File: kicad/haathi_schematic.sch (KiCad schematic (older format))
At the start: 0 parts

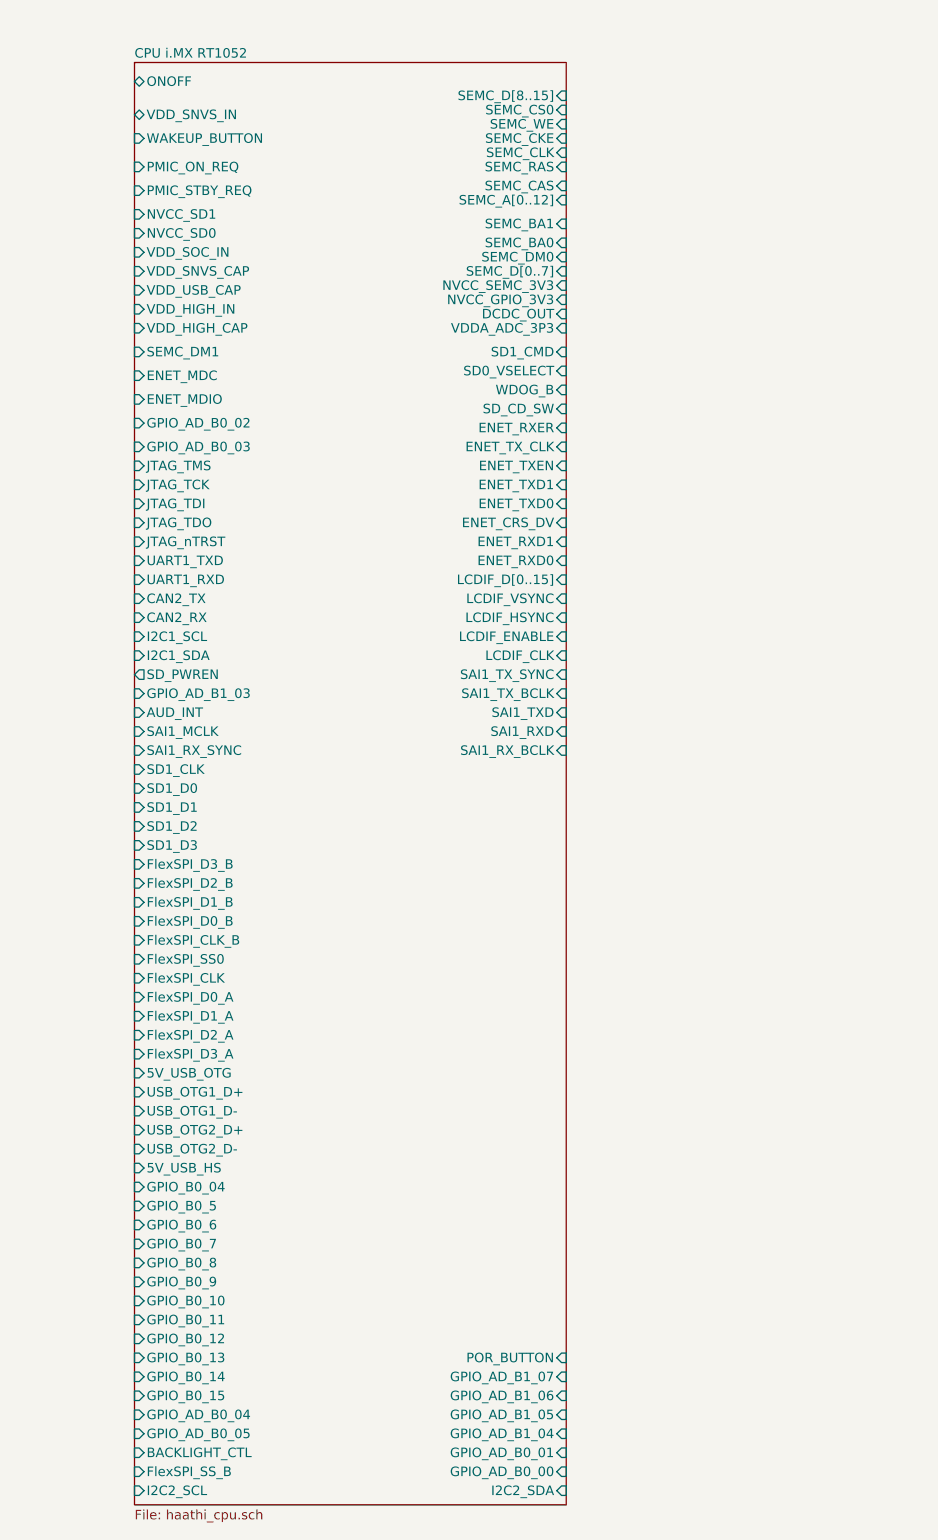
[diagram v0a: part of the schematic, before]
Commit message: Top schematic, re-arranged CPU block pins and added wires
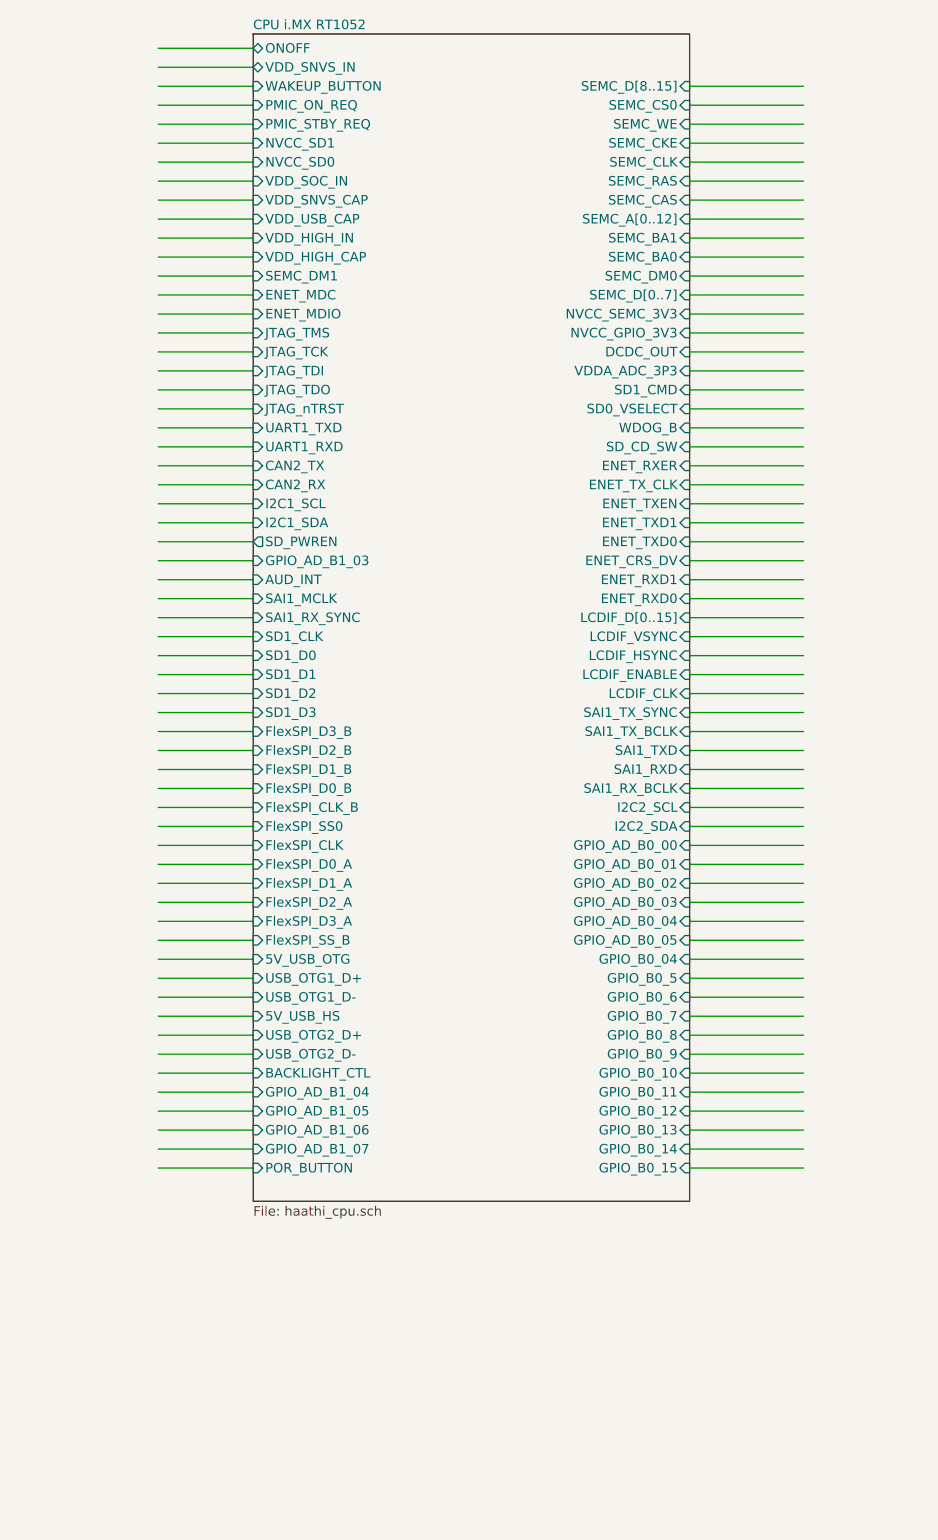
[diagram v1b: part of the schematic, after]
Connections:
- wire segments 5 -> 123

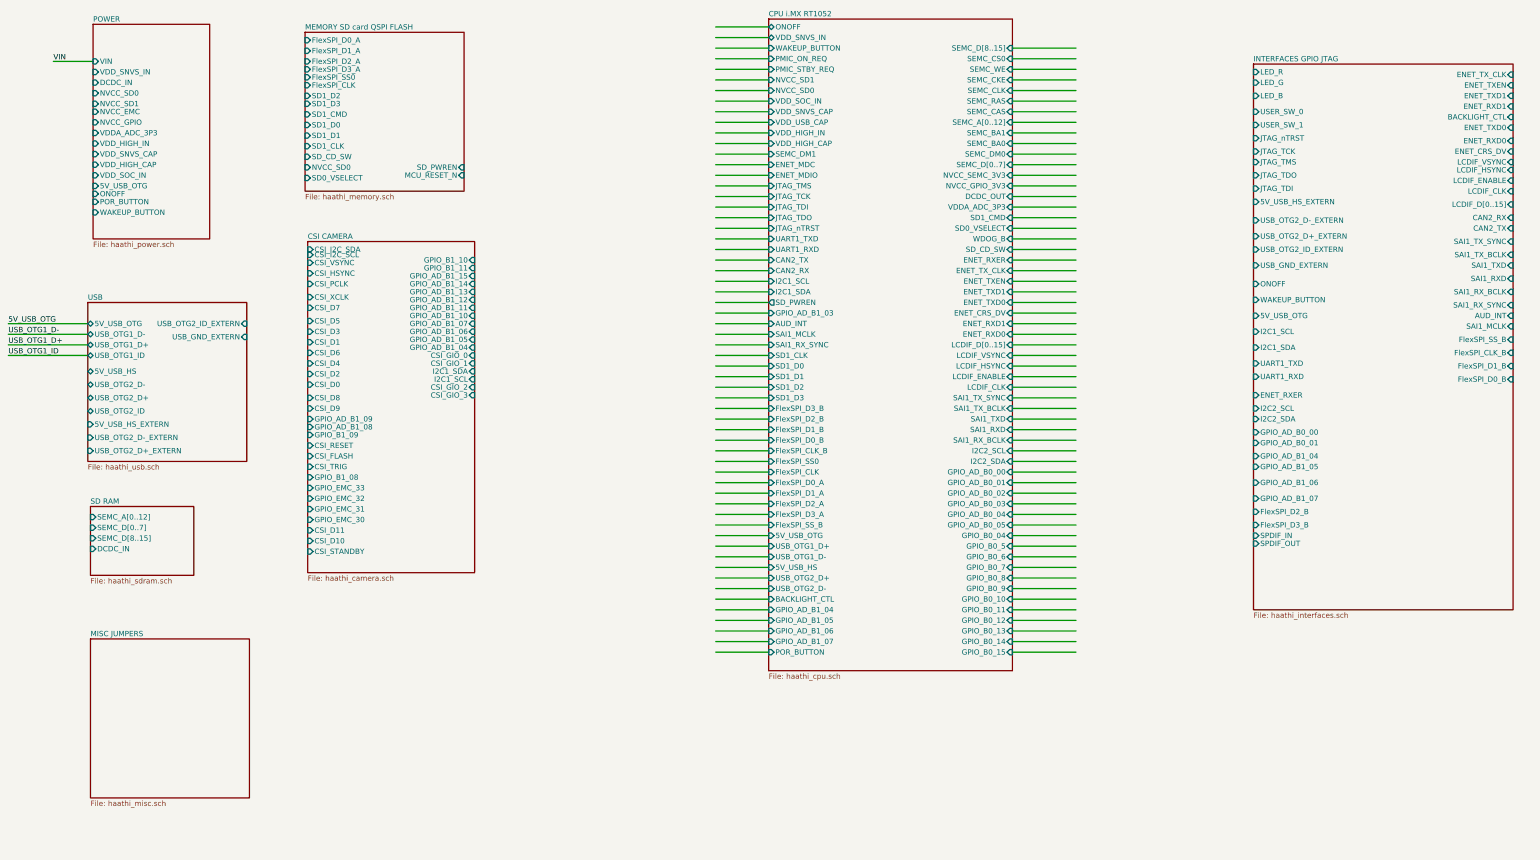
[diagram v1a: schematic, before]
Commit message: CPU, Interfaces, SDRAM top sheet wiring done, CPU bootcfg local labels fixed
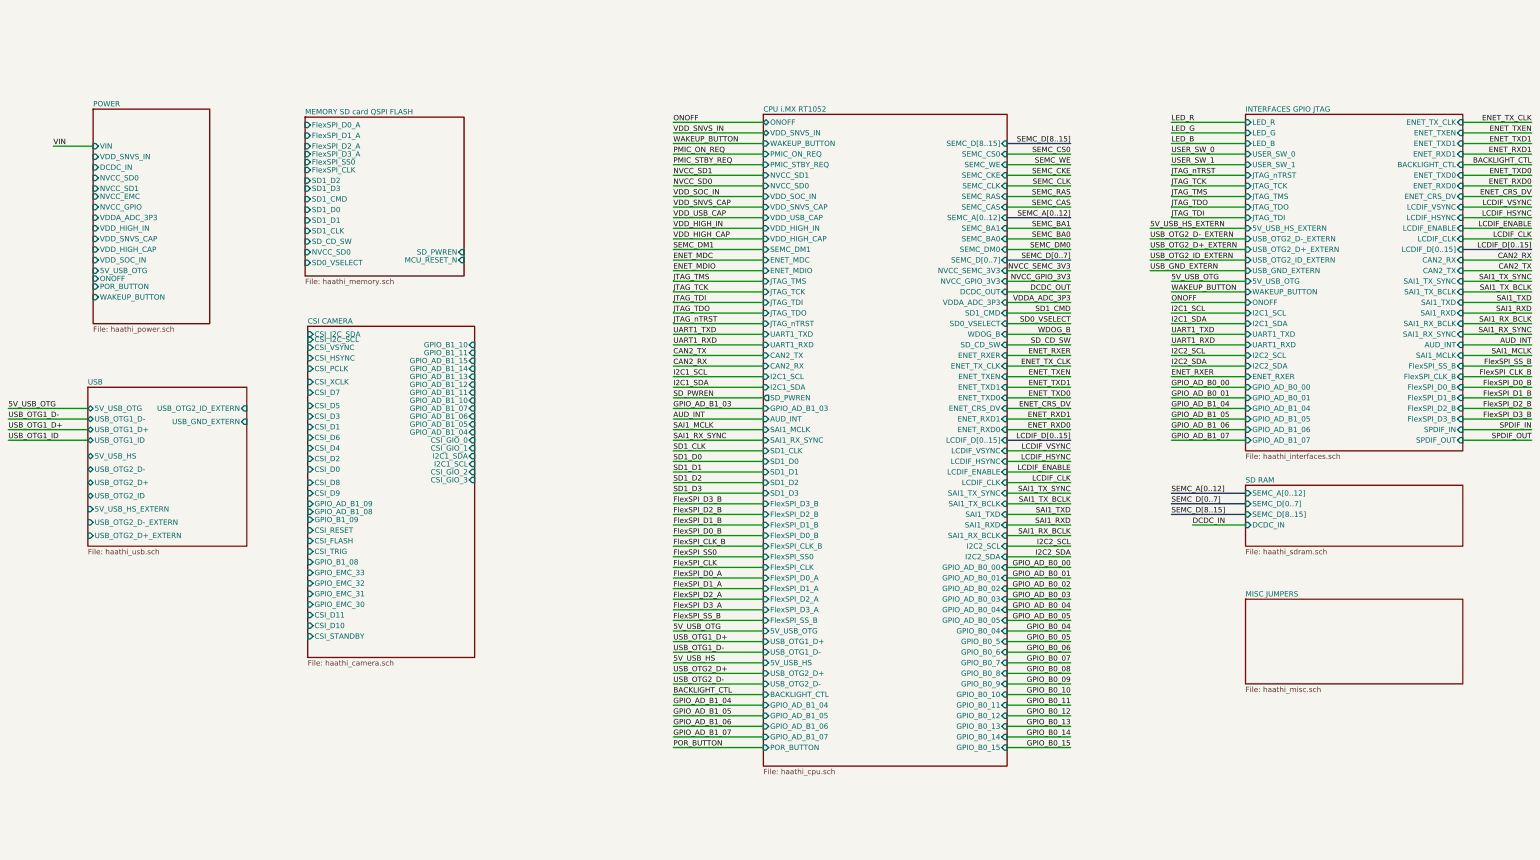
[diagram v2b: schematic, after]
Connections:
- net labels added: 5V_USB_HS, 5V_USB_HS_EXTERN, AUD_INT, BACKLIGHT_CTL, CAN2_RX, CAN2_TX, DCDC_IN, DCDC_OUT, ENET_CRS_DV, ENET_MDC, ENET_MDIO, ENET_RXD0, ENET_RXD1, ENET_RXER, ENET_TXD0, ENET_TXD1, ENET_TXEN, ENET_TX_CLK, FlexSPI_CLK, FlexSPI_CLK_B, FlexSPI_D0_A, FlexSPI_D0_B, FlexSPI_D1_A, FlexSPI_D1_B, FlexSPI_D2_A, FlexSPI_D2_B, FlexSPI_D3_A, FlexSPI_D3_B, FlexSPI_SS0, FlexSPI_SS_B, GPIO_AD_B0_00, GPIO_AD_B0_01, GPIO_AD_B0_02, GPIO_AD_B0_03, GPIO_AD_B0_04, GPIO_AD_B0_05, GPIO_AD_B1_03, GPIO_AD_B1_04, GPIO_AD_B1_05, GPIO_AD_B1_06, GPIO_AD_B1_07, GPIO_B0_04, GPIO_B0_05, GPIO_B0_06, GPIO_B0_07, GPIO_B0_08, GPIO_B0_09, GPIO_B0_10, GPIO_B0_11, GPIO_B0_12, GPIO_B0_13, GPIO_B0_14, GPIO_B0_15, I2C1_SCL, I2C1_SDA, I2C2_SCL, I2C2_SDA, JTAG_TCK, JTAG_TDI, JTAG_TDO, JTAG_TMS, JTAG_nTRST, LCDIF_CLK, LCDIF_D[0..15], LCDIF_ENABLE, LCDIF_HSYNC, LCDIF_VSYNC, LED_B, LED_G, LED_R, NVCC_GPIO_3V3, NVCC_SD0, NVCC_SD1, NVCC_SEMC_3V3, ONOFF, PMIC_ON_REQ, PMIC_STBY_REQ, POR_BUTTON, SAI1_MCLK, SAI1_RXD, SAI1_RX_BCLK, SAI1_RX_SYNC, SAI1_TXD, SAI1_TX_BCLK, SAI1_TX_SYNC, SD0_VSELECT, SD1_CLK, SD1_CMD, SD1_D0, SD1_D1, SD1_D2, SD1_D3, SD_CD_SW, SD_PWREN, SEMC_A[0..12], SEMC_BA0, SEMC_BA1, SEMC_CAS, SEMC_CKE, SEMC_CLK, SEMC_CS0, SEMC_DM0, SEMC_DM1, SEMC_D[0..7], SEMC_D[8..15], SEMC_RAS, SEMC_WE, SPDIF_IN, SPDIF_OUT, UART1_RXD, UART1_TXD, USB_GND_EXTERN, USB_OTG2_D+, USB_OTG2_D+_EXTERN, USB_OTG2_D-, USB_OTG2_D-_EXTERN, USB_OTG2_ID_EXTERN, USER_SW_0, USER_SW_1, VDDA_ADC_3P3, VDD_HIGH_CAP, VDD_HIGH_IN, VDD_SNVS_CAP, VDD_SNVS_IN, VDD_SOC_IN, VDD_USB_CAP, WAKEUP_BUTTON, WDOG_B
- wire segments 123 -> 181

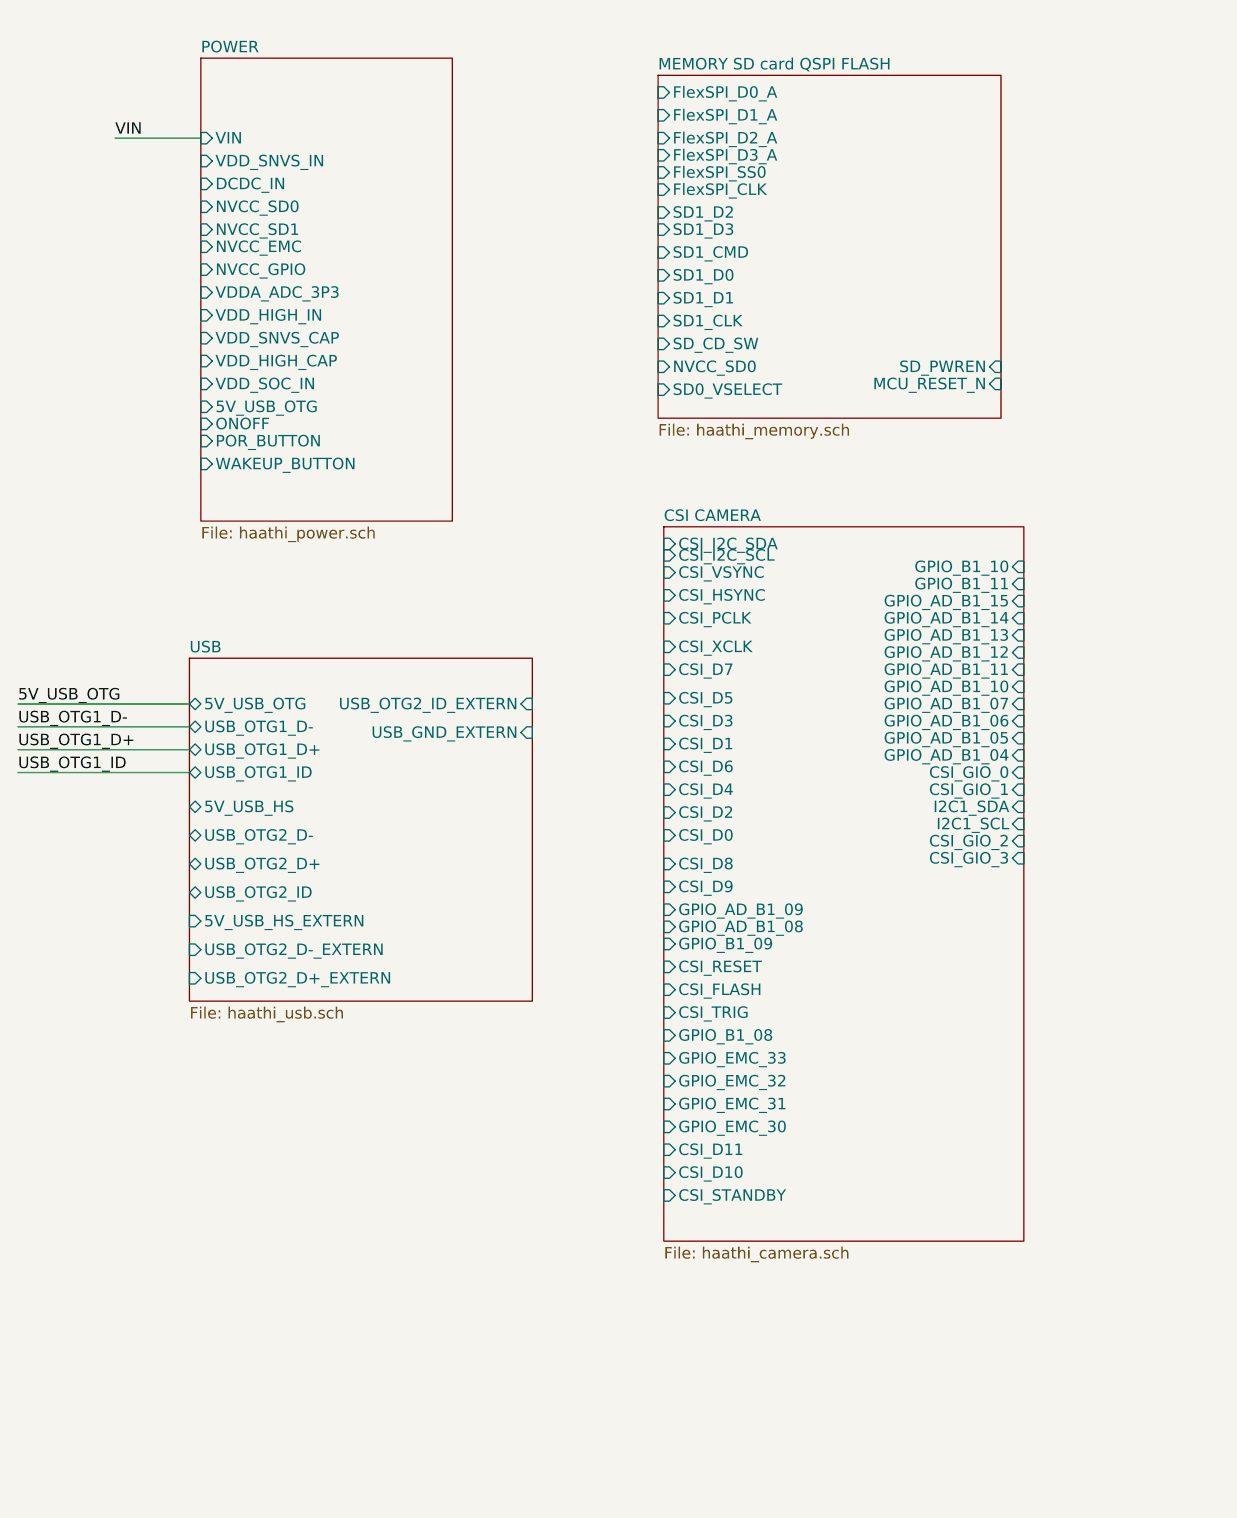
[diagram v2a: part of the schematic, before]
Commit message: haathi_schematic: Rearange hier-labels and complete schematic wiring
Signed-off-by: Kumar Abhishek <abhishek@theembeddedkitchen.net>
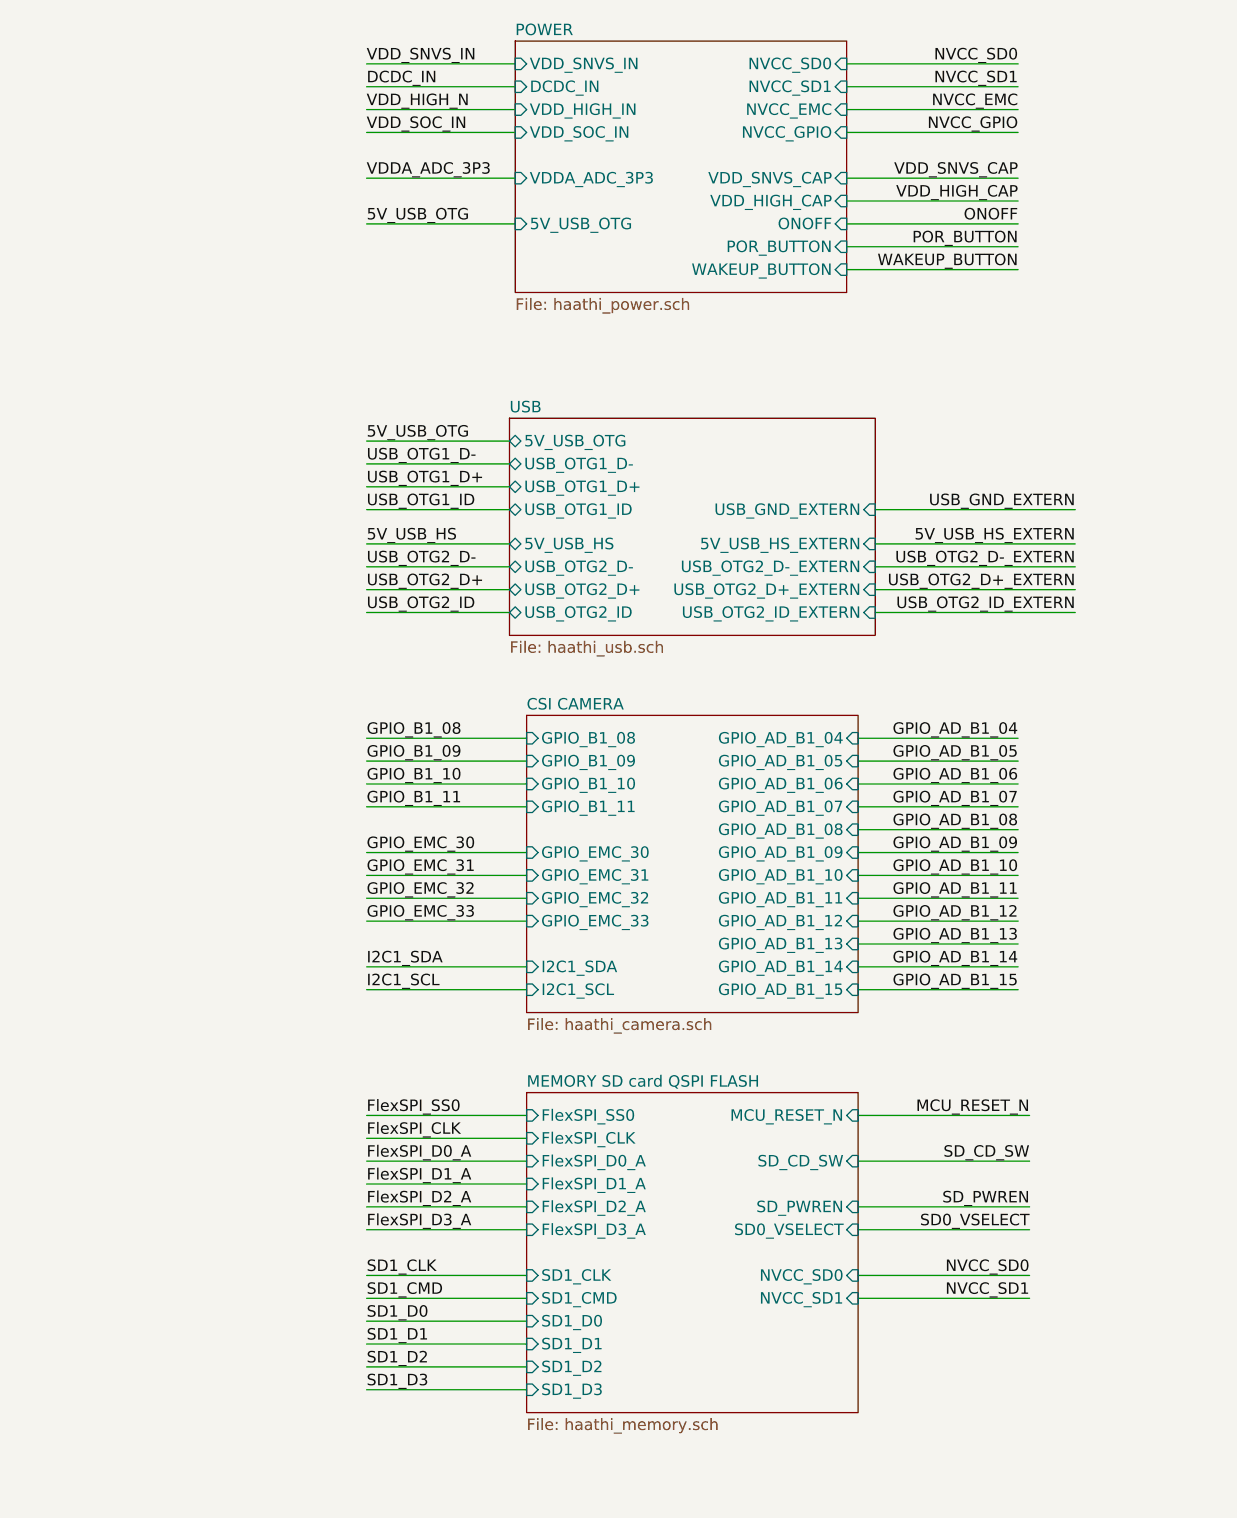
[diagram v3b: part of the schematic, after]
